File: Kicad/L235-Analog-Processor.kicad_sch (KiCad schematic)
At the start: 224 parts, among them IC1 CA3046Z, J1 Input A, J10 Half Wave In B, J11 Inverted Out B, J12 Invert IN B, J13 Invert IN A, J14 Half Wave In A, J15 Inverted Out A, J16 Full-Wave Rectifier A, J17 Half-Wave Rectifier A, J18 √(A²+B²), J19 A * B / 10, J2 Input B, J3 Argument Filter X Out, J4 10A / |B|, J5 Output F(x), J6 Power, J7 Full-Wave Rectifier B, J8 A - B, J9 Half-Wave Rectifier B, Q1 NPN, SW1 71BF30-02-2-06N-circular, SW2 INVERT SWITCH, SW3 71BF30-02-2-06N-circular, SW4 FULL/HALF WAVE, SW5 SW_Rotary_1x8_MP, SW6 ADD/SUBTRACT, SW7 POS/NEG HALF WAVE, U1 TL082, U10 TL082, U11 TL082, U12 TL082, U13 TL084, U14 CA3046Z, U15 TL082, U16 AD534LDZ, U17 TL082, U18 TL082, U19 TL082, U2 TL082, U3 TL082, U4 TL082, U5 TL082, U6 TL082, U7 TL082, U8 TL082, U9 TL082

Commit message: Fixed symbol pins AD534JH, Added IC power Rectifier/Inverse
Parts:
- removed R60: 50k, Resistor_THT:R_Axial_DIN0614_L14.3mm_D5.7mm_P15.24mm_Horizontal, symbol Device:R
- removed R61: 20k, Resistor_THT:R_Axial_DIN0614_L14.3mm_D5.7mm_P15.24mm_Horizontal, symbol Device:R
- removed R62: 10k, Resistor_THT:R_Axial_DIN0614_L14.3mm_D5.7mm_P15.24mm_Horizontal, symbol Device:R
- removed R63: 5k, Resistor_THT:R_Axial_DIN0614_L14.3mm_D5.7mm_P15.24mm_Horizontal, symbol Device:R
- removed R64: 2k, Resistor_THT:R_Axial_DIN0614_L14.3mm_D5.7mm_P15.24mm_Horizontal, symbol Device:R
- removed R65: 1k, Resistor_THT:R_Axial_DIN0614_L14.3mm_D5.7mm_P15.24mm_Horizontal, symbol Device:R
- removed R66: 500, Resistor_THT:R_Axial_DIN0614_L14.3mm_D5.7mm_P15.24mm_Horizontal, symbol Device:R
- removed R90: 180, Resistor_THT:R_Axial_DIN0614_L14.3mm_D5.7mm_P15.24mm_Horizontal, symbol Device:R
- removed SW5: SW_Rotary_1x8_MP, symbol Switch:SW_Rotary_1x8_MP
- removed TP1: X, TestPoint:TestPoint_THTPad_2.0x2.0mm_Drill1.0mm, symbol Connector:TestPoint
- removed TP2: <X>, TestPoint:TestPoint_THTPad_2.0x2.0mm_Drill1.0mm, symbol Connector:TestPoint
- removed TP4: |A|, TestPoint:TestPoint_THTPad_2.0x2.0mm_Drill1.0mm, symbol Connector:TestPoint
- added C4, C40, C41, C42: 100nF, Capacitor_THT:C_Rect_L7.0mm_W3.5mm_P2.50mm_P5.00mm, symbol Device:C
- added J20, J21: Root Input |A|, Connector_Audio:Jack_3.5mm_PJ311_Horizontal, symbol Connector_Audio:AudioJack2_Ground_SwitchT
- added R100, R95, R96, R97, R98, R99: 100k, Resistor_THT:R_Axial_DIN0614_L14.3mm_D5.7mm_P15.24mm_Horizontal, symbol Device:R
- added RV8: 100k, Resistor_THT:R_Axial_DIN0614_L14.3mm_D5.7mm_P15.24mm_Horizontal, symbol Device:R_Potentiometer_Trim
- added SW8: INVERT SWITCH, symbol Switch:SW_SPDT
- added unit 3 of U14
- added unit 3 of U15
- J3: value Argument Filter X Out -> Function IN
- R2, R4: value 1M -> 100k
- U16: value AD534LDZ -> AD534JH
- renumbered U15 to U14, U18 to U14, U17 to U15, U19 to U15
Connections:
- net +12V: now also R59.1, U14.3 (+), U15.3 (+), U16.3 (Y1), U16.5 (-VS), U16.9 (+VS), J20.G, J21.G, R100.1, R95.1, R96.1, R97.1, R98.1, R99.1; no longer U14.5 (+), U15.5 (+), U16.14 (+VS), U16.6 (Y1), U16.8 (-VS)
- net <X>: now also J3.T, R59.2; no longer U7.6 (-), U7.7
- net |A|: no longer D5.1 (K), D8.1 (K), R21.1, R5.2, R6.2, R88.1
- net at D12.2 (A), D17.1 (K), SW3.C11: now also RV8.1
- net at R15.1, R91.2, R94.2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: now also U16.8 (OUT); no longer U16.12 (OUT)
- net at R67.2, U12.6 (-): now also RV8.2, RV8.3; no longer R59.1
- net at J14.TN, R16.1, R19.1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: now also SW8.2 (B); no longer U1.1, U1.2 (-)
- net at R16.2, SW1.B1, SW1.B2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: now also U16.6 (Z2); no longer U16.10 (Z2)
- net at R83.2, R84.1: now also U14.2 (-); no longer U14.6 (-)
- net at R84.2, R87.2: now also U14.1, SW8.1 (A); no longer U14.7
- net at J10.T, R34.1: now also R98.2
- net at J12.T, R38.1: now also R97.2
- net at R17.2, R18.1: now also U16.10 (X1); no longer U16.1 (X1)
- net at R15.2, SW1.B4: now also U16.7 (Z1); no longer U16.11 (Z1)
- net at SW1.C22: now also U16.1 (X2); no longer U16.2 (X2)
- net at U16.4 (Y2): now also SW1.C12
- net at J13.T, R83.1: now also R95.2
- net at D31.2 (A), R85.2, R86.1: now also U15.2 (-); no longer U15.6 (-)
- net at J3.TN: now also U7.6 (-), U7.7
- net at J14.T, R85.1: now also R96.2
- net at D31.1 (K), D32.2 (A): now also U15.1; no longer U15.7
- net at RV3.2, RV3.3: now also J21.T, R100.2; no longer R13.1, SW4.2 (B)
- new net: J20.T, R21.1, R99.2
- new net: C4.1, C41.1, U14.8 (V+), U15.8 (V+)
- new net: C4.2, C41.2
- new net: C40.2, C42.2, U14.4 (V-), U15.4 (V-)
- new net: D5.1 (K), D8.1 (K), J20.TN, R5.2, R6.2, R88.1
- new net: SW8.3 (C), U1.1, U1.2 (-)
- new net: C40.1, C42.1
- new net: J21.TN, R13.1, SW4.2 (B)
- no-connect marks 53 -> 51
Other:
- note added: "-dX/dt"
- note added: "-dX/dt*1/100"
- note added: "<X>"
- note added: "Argument Filter"
- note added: "OUTPUT GAIN"
- note added: "X"
- note added: "X²"
- moved on the sheet: C3, J1, J13, J19, J3, J4, J8, R1, R2, R83, R84, R91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

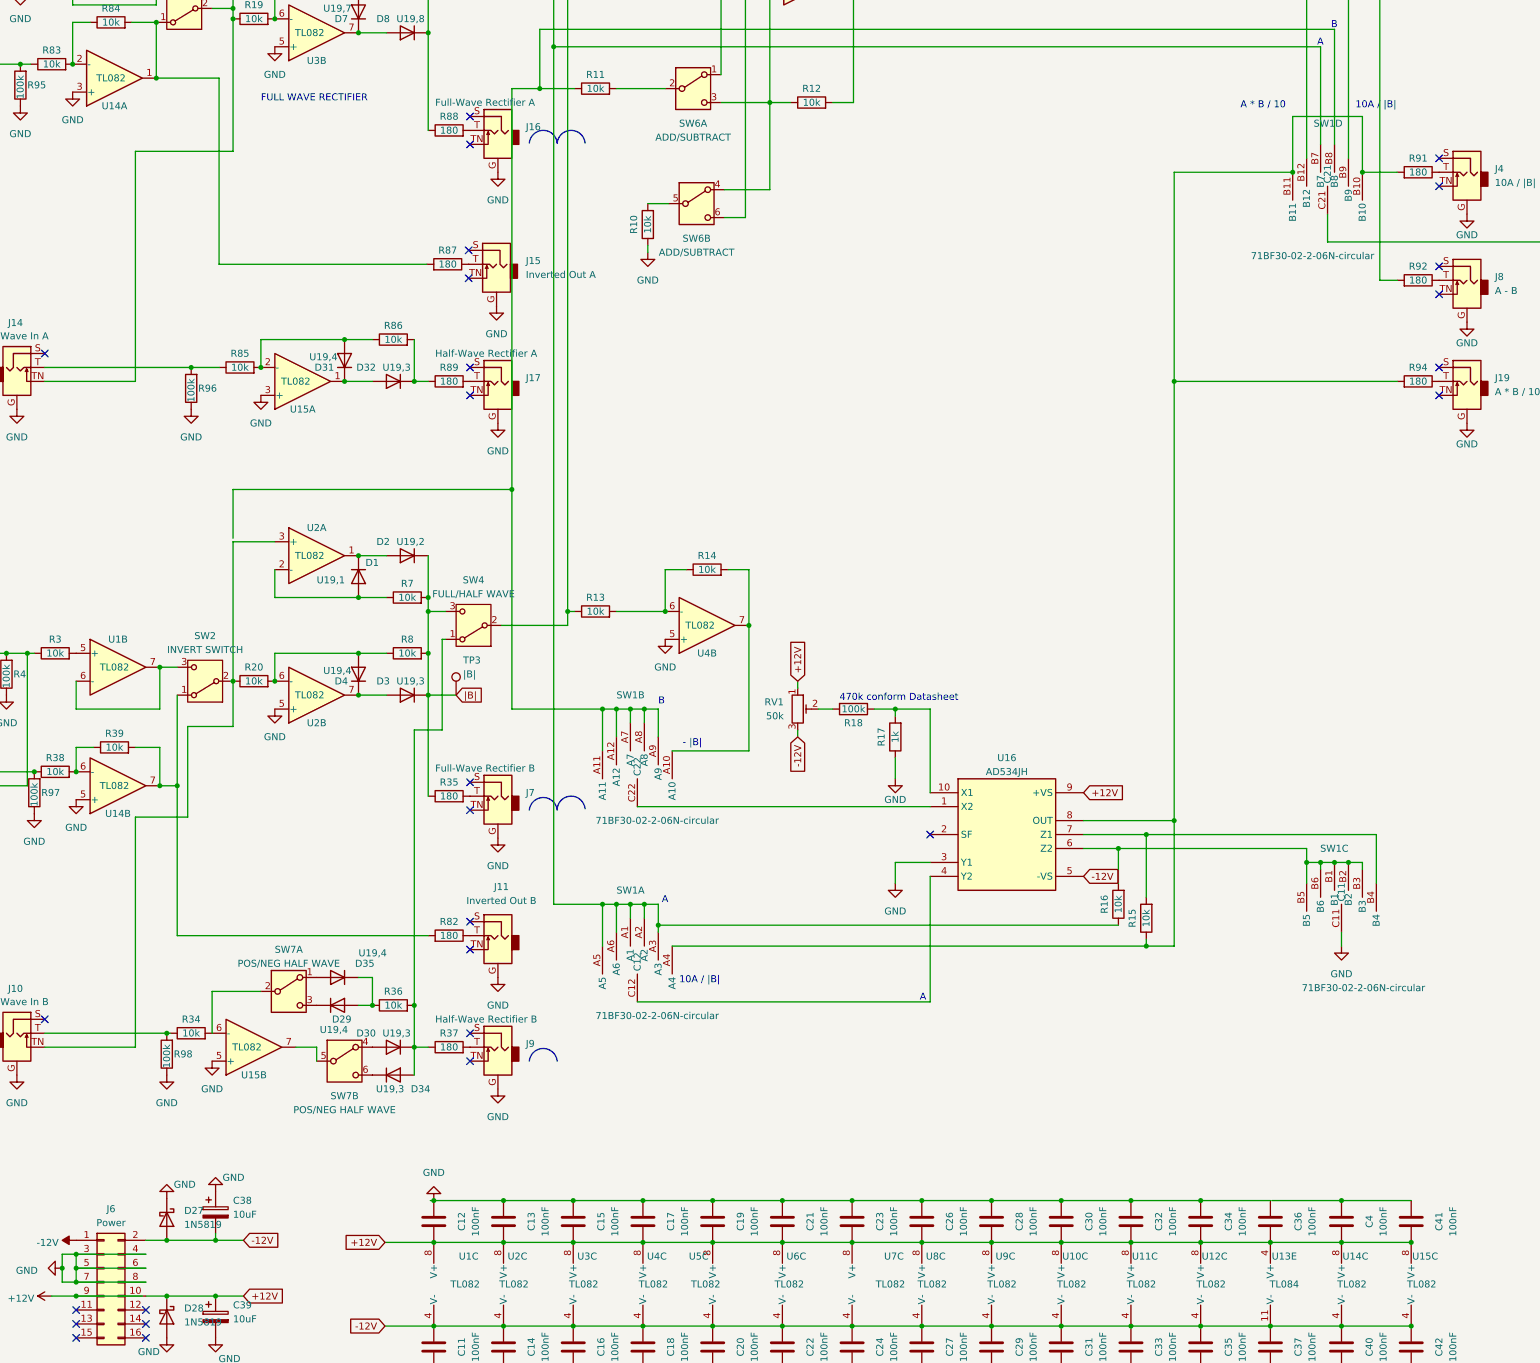
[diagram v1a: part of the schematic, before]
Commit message: fixed double U14 annotation
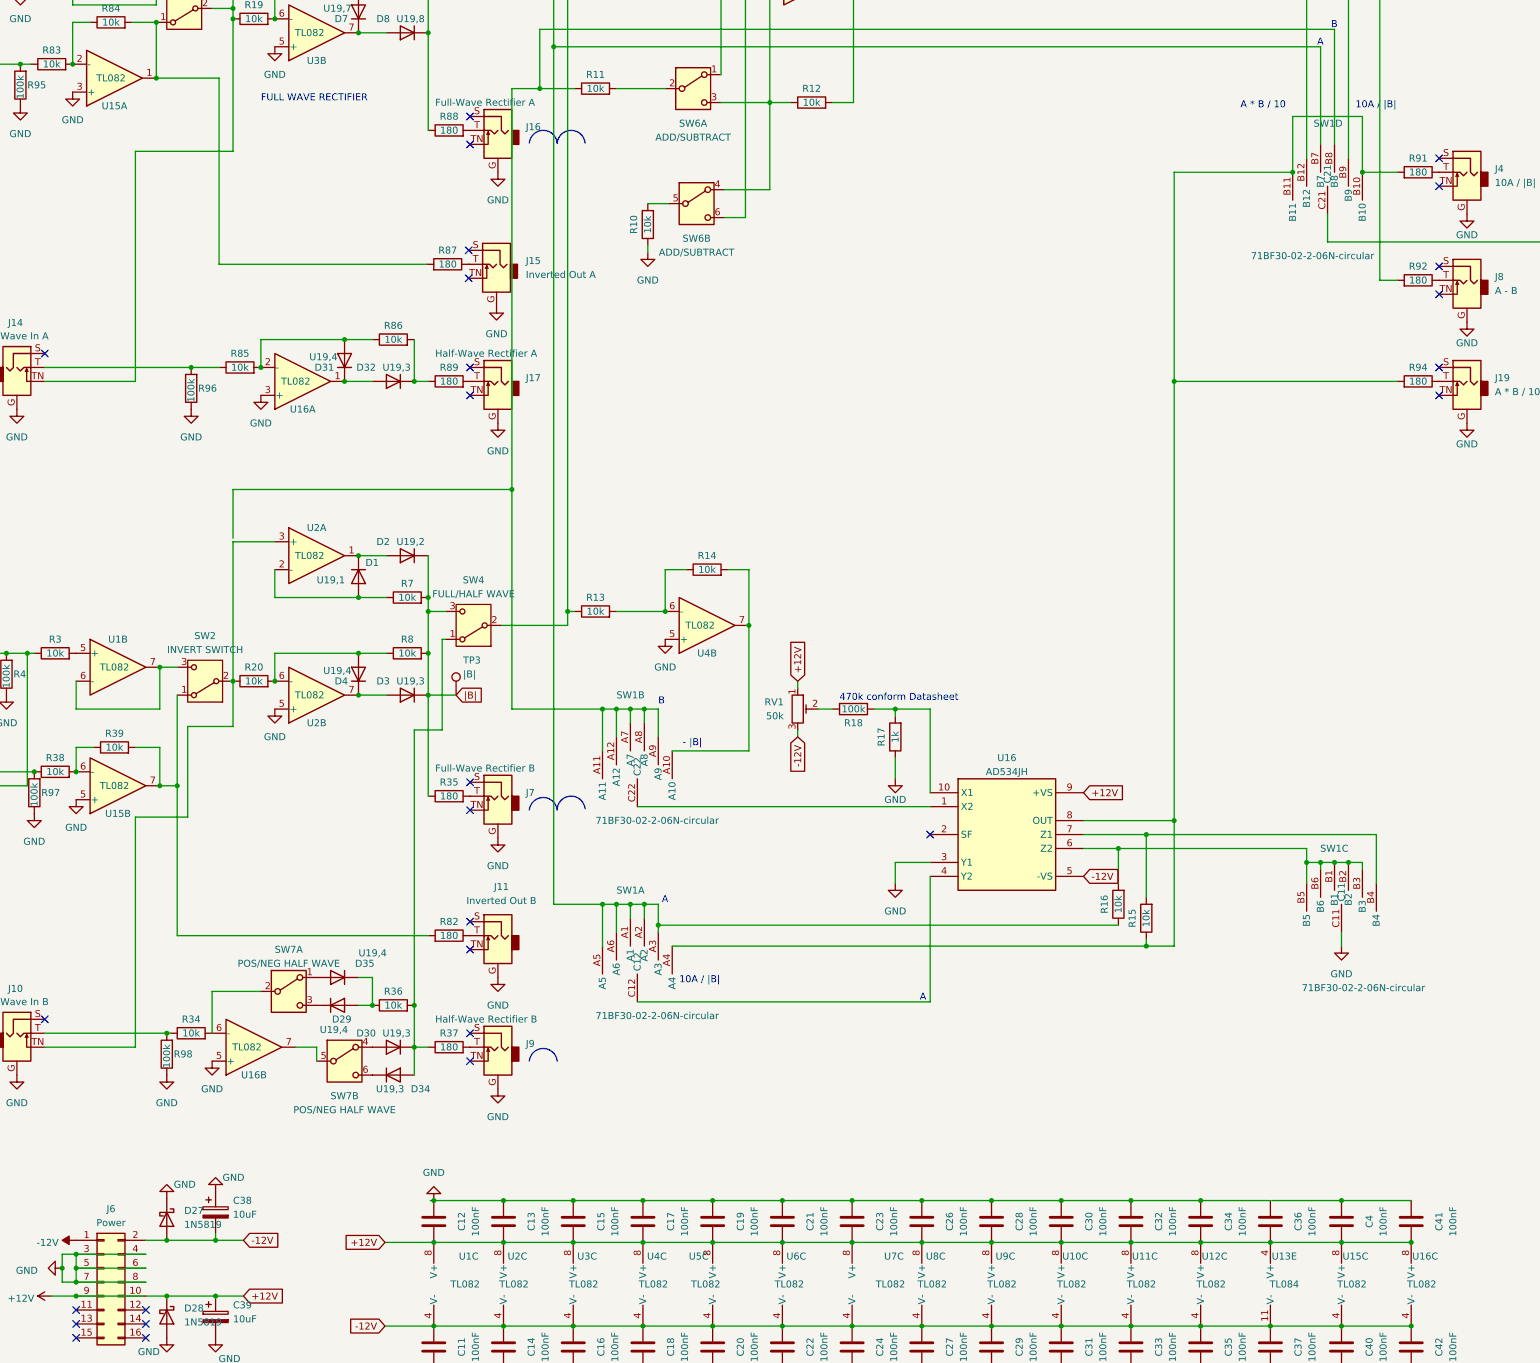
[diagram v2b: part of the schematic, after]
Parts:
- renumbered U14 to U15, U15 to U16
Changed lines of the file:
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@@
   (symbol (lib_id "Amplifier_Operational:TL082") (at 287.02 365.76 0) (unit 3)
     (in_bom yes) (on_board yes) (dnp no)
-    (property "Reference" "U15" (at 287.02 360.68 0)
+    (property "Reference" "U16" (at 287.02 360.68 0)
       (effects (font (size 1.27 1.27)))
     )
@@
       (project "L235-Analog-Processor"
         (path "/11565f7a-671a-4a91-8d3b-c6d6401f938b"
-          (reference "U15") (unit 3)
+          (reference "U16") (unit 3)
         )
       )
@@
   (symbol (lib_id "Amplifier_Operational:TL082") (at 73.66 322.58 0) (mirror x) (unit 2)
     (in_bom yes) (on_board yes) (dnp no)
-    (property "Reference" "U15" (at 73.66 327.66 0)
+    (property "Reference" "U16" (at 73.66 327.66 0)
       (effects (font (size 1.27 1.27)))
     )
@@
       (project "L235-Analog-Processor"
         (path "/11565f7a-671a-4a91-8d3b-c6d6401f938b"
-          (reference "U15") (unit 2)
+          (reference "U16") (unit 2)
         )
       )
@@
   (symbol (lib_id "Amplifier_Operational:TL082") (at 48.895 274.955 0) (mirror x) (unit 2)
     (in_bom yes) (on_board yes) (dnp no)
-    (property "Reference" "U14" (at 48.895 280.035 0)
+    (property "Reference" "U15" (at 48.895 280.035 0)
       (effects (font (size 1.27 1.27)))
     )
@@
       (project "L235-Analog-Processor"
         (path "/11565f7a-671a-4a91-8d3b-c6d6401f938b"
-          (reference "U14") (unit 2)
+          (reference "U15") (unit 2)
         )
       )
@@
   (symbol (lib_id "Amplifier_Operational:TL082") (at 82.55 201.295 0) (mirror x) (unit 1)
     (in_bom yes) (on_board yes) (dnp no)
-    (property "Reference" "U15" (at 82.55 206.375 0)
+    (property "Reference" "U16" (at 82.55 206.375 0)
       (effects (font (size 1.27 1.27)))
     )
@@
       (project "L235-Analog-Processor"
         (path "/11565f7a-671a-4a91-8d3b-c6d6401f938b"
-          (reference "U15") (unit 1)
+          (reference "U16") (unit 1)
         )
       )
@@
   (symbol (lib_id "Amplifier_Operational:TL082") (at 48.26 146.05 0) (mirror x) (unit 1)
     (in_bom yes) (on_board yes) (dnp no)
-    (property "Reference" "U14" (at 48.26 151.13 0)
+    (property "Reference" "U15" (at 48.26 151.13 0)
       (effects (font (size 1.27 1.27)))
     )
@@
       (project "L235-Analog-Processor"
         (path "/11565f7a-671a-4a91-8d3b-c6d6401f938b"
-          (reference "U14") (unit 1)
+          (reference "U15") (unit 1)
         )
       )
@@
   (symbol (lib_id "Amplifier_Operational:TL082") (at 274.32 365.76 0) (unit 3)
     (in_bom yes) (on_board yes) (dnp no)
-    (property "Reference" "U14" (at 274.32 360.68 0)
+    (property "Reference" "U15" (at 274.32 360.68 0)
       (effects (font (size 1.27 1.27)))
     )
@@
       (project "L235-Analog-Processor"
         (path "/11565f7a-671a-4a91-8d3b-c6d6401f938b"
-          (reference "U14") (unit 3)
+          (reference "U15") (unit 3)
         )
       )
